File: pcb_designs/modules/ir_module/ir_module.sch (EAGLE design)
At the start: 10 parts, among them IC1 358

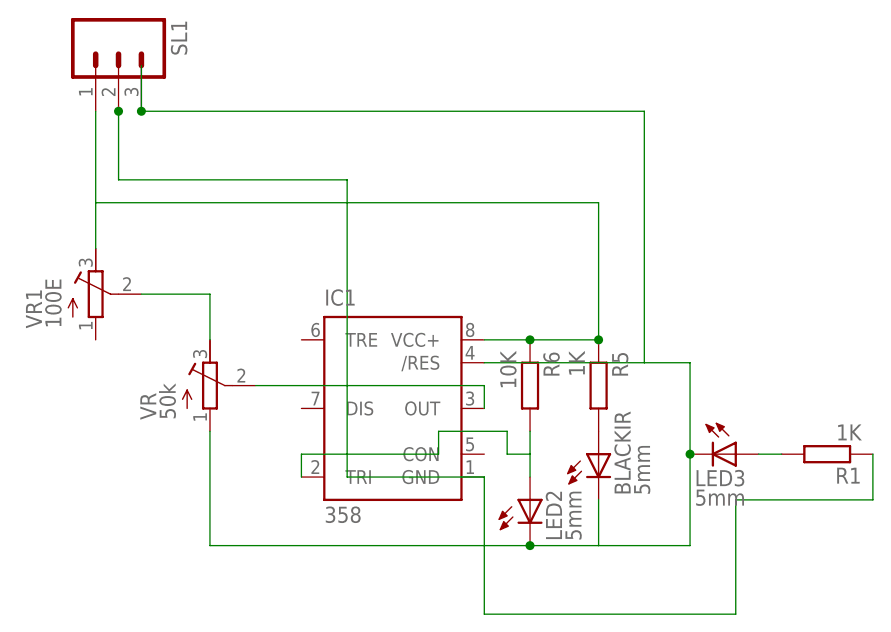
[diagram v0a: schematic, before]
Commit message: 
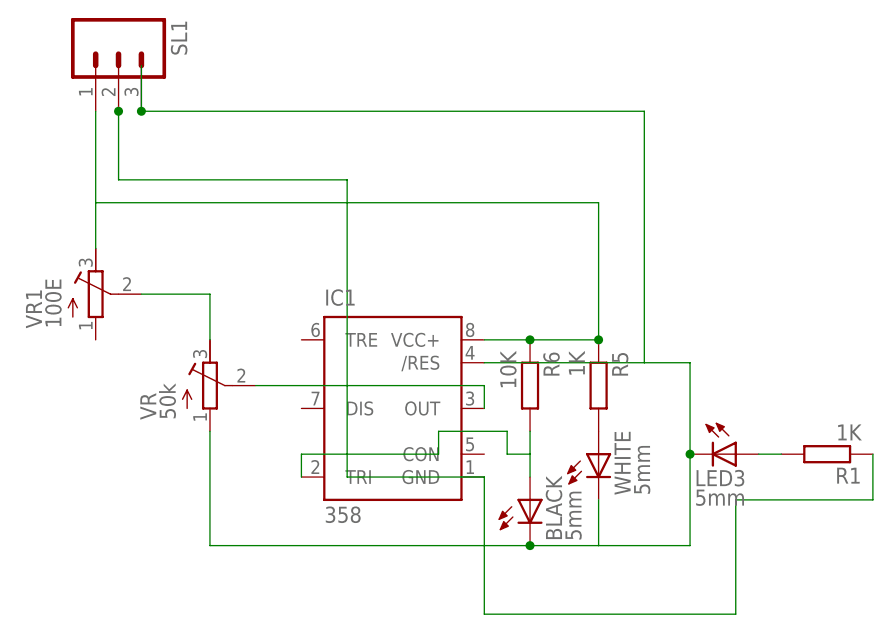
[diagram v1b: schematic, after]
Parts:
- renumbered BLACKIR to WHITE, LED2 to BLACK
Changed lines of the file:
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@@
 <part name="R1" library="rcl" deviceset="R-EU_" device="0204/7" value="1K"/>
 <part name="VR" library="resistor" deviceset="R-TRIMM" device="64P" value="50k"/>
-<part name="BLACKIR" library="led" deviceset="LED" device="5MM" value="5mm"/>
+<part name="WHITE" library="led" deviceset="LED" device="5MM" value="5mm"/>
 <part name="SL1" library="con-amp-quick" deviceset="M03" device=""/>
-<part name="LED2" library="led" deviceset="LED" device="5MM" value="5mm"/>
+<part name="BLACK" library="led" deviceset="LED" device="5MM" value="5mm"/>
 <part name="LED3" library="led" deviceset="LED" device="5MM" value="5mm"/>
 <part name="R5" library="rcl" deviceset="R-EU_" device="0204/7" value="1K"/>
@@
 <instance part="R1" gate="G$1" x="101.6" y="40.64" rot="R180"/>
 <instance part="VR" gate="G$1" x="33.02" y="48.26"/>
-<instance part="BLACKIR" gate="G$1" x="76.2" y="40.64"/>
+<instance part="WHITE" gate="G$1" x="76.2" y="40.64"/>
 <instance part="SL1" gate="G$1" x="22.86" y="86.36" rot="R270"/>
-<instance part="LED2" gate="G$1" x="68.58" y="35.56"/>
+<instance part="BLACK" gate="G$1" x="68.58" y="35.56"/>
 <instance part="LED3" gate="G$1" x="91.44" y="40.64" rot="R270"/>
 <instance part="R5" gate="G$1" x="76.2" y="48.26" rot="R270"/>
@@
 <segment>
 <pinref part="R5" gate="G$1" pin="2"/>
-<pinref part="BLACKIR" gate="G$1" pin="A"/>
+<pinref part="WHITE" gate="G$1" pin="A"/>
 </segment>
 </net>
@@
 <segment>
 <pinref part="R6" gate="G$1" pin="2"/>
-<pinref part="LED2" gate="G$1" pin="A"/>
+<pinref part="BLACK" gate="G$1" pin="A"/>
 <wire x1="68.58" y1="38.1" x2="68.58" y2="40.64" width="0.1524" layer="91"/>
 <wire x1="68.58" y1="40.64" x2="68.58" y2="43.18" width="0.1524" layer="91"/>
@@
 <net name="N$11" class="0">
 <segment>
-<pinref part="BLACKIR" gate="G$1" pin="C"/>
+<pinref part="WHITE" gate="G$1" pin="C"/>
 <wire x1="76.2" y1="30.48" x2="76.2" y2="35.56" width="0.1524" layer="91"/>
 <wire x1="68.58" y1="30.48" x2="76.2" y2="30.48" width="0.1524" layer="91"/>
-<pinref part="LED2" gate="G$1" pin="C"/>
+<pinref part="BLACK" gate="G$1" pin="C"/>
 <junction x="68.58" y="30.48"/>
 <pinref part="VR" gate="G$1" pin="E"/>

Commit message: 
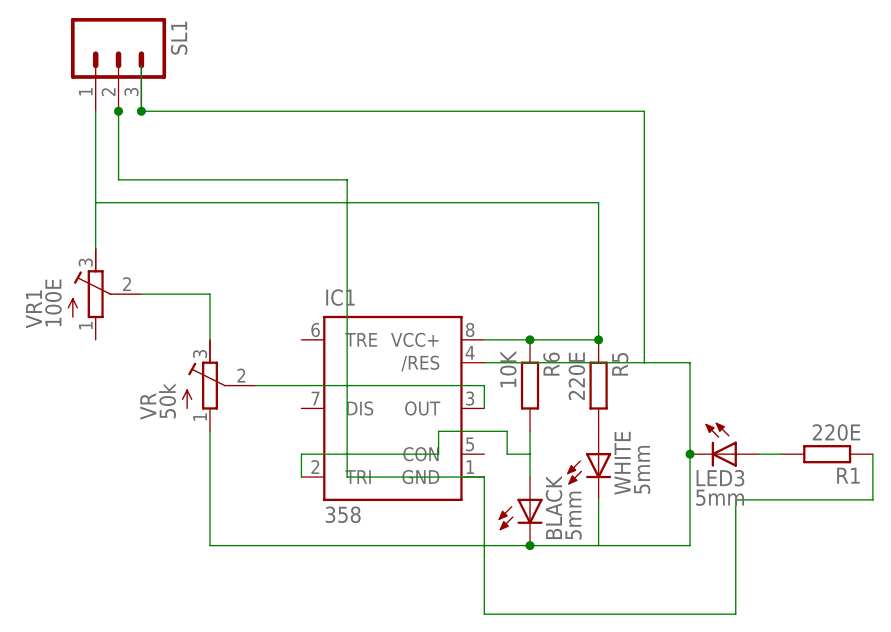
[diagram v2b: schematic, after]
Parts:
- R1, R5: value 1K -> 220E
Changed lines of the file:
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@@
 <parts>
 <part name="IC1" library="st-microelectronics" deviceset="NE555" device="" value="358"/>
-<part name="R1" library="rcl" deviceset="R-EU_" device="0204/7" value="1K"/>
+<part name="R1" library="rcl" deviceset="R-EU_" device="0204/7" value="220E"/>
 <part name="VR" library="resistor" deviceset="R-TRIMM" device="64P" value="50k"/>
 <part name="WHITE" library="led" deviceset="LED" device="5MM" value="5mm"/>
@@
 <part name="BLACK" library="led" deviceset="LED" device="5MM" value="5mm"/>
 <part name="LED3" library="led" deviceset="LED" device="5MM" value="5mm"/>
-<part name="R5" library="rcl" deviceset="R-EU_" device="0204/7" value="1K"/>
+<part name="R5" library="rcl" deviceset="R-EU_" device="0204/7" value="220E"/>
 <part name="R6" library="rcl" deviceset="R-EU_" device="0204/7" value="10K"/>
 <part name="VR1" library="resistor" deviceset="R-TRIMM" device="64P" value="100E"/>
